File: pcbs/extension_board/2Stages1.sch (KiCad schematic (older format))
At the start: 12 parts, among them Q1 MMBT3904, Q2 MMBT3904, U1 LM324QT

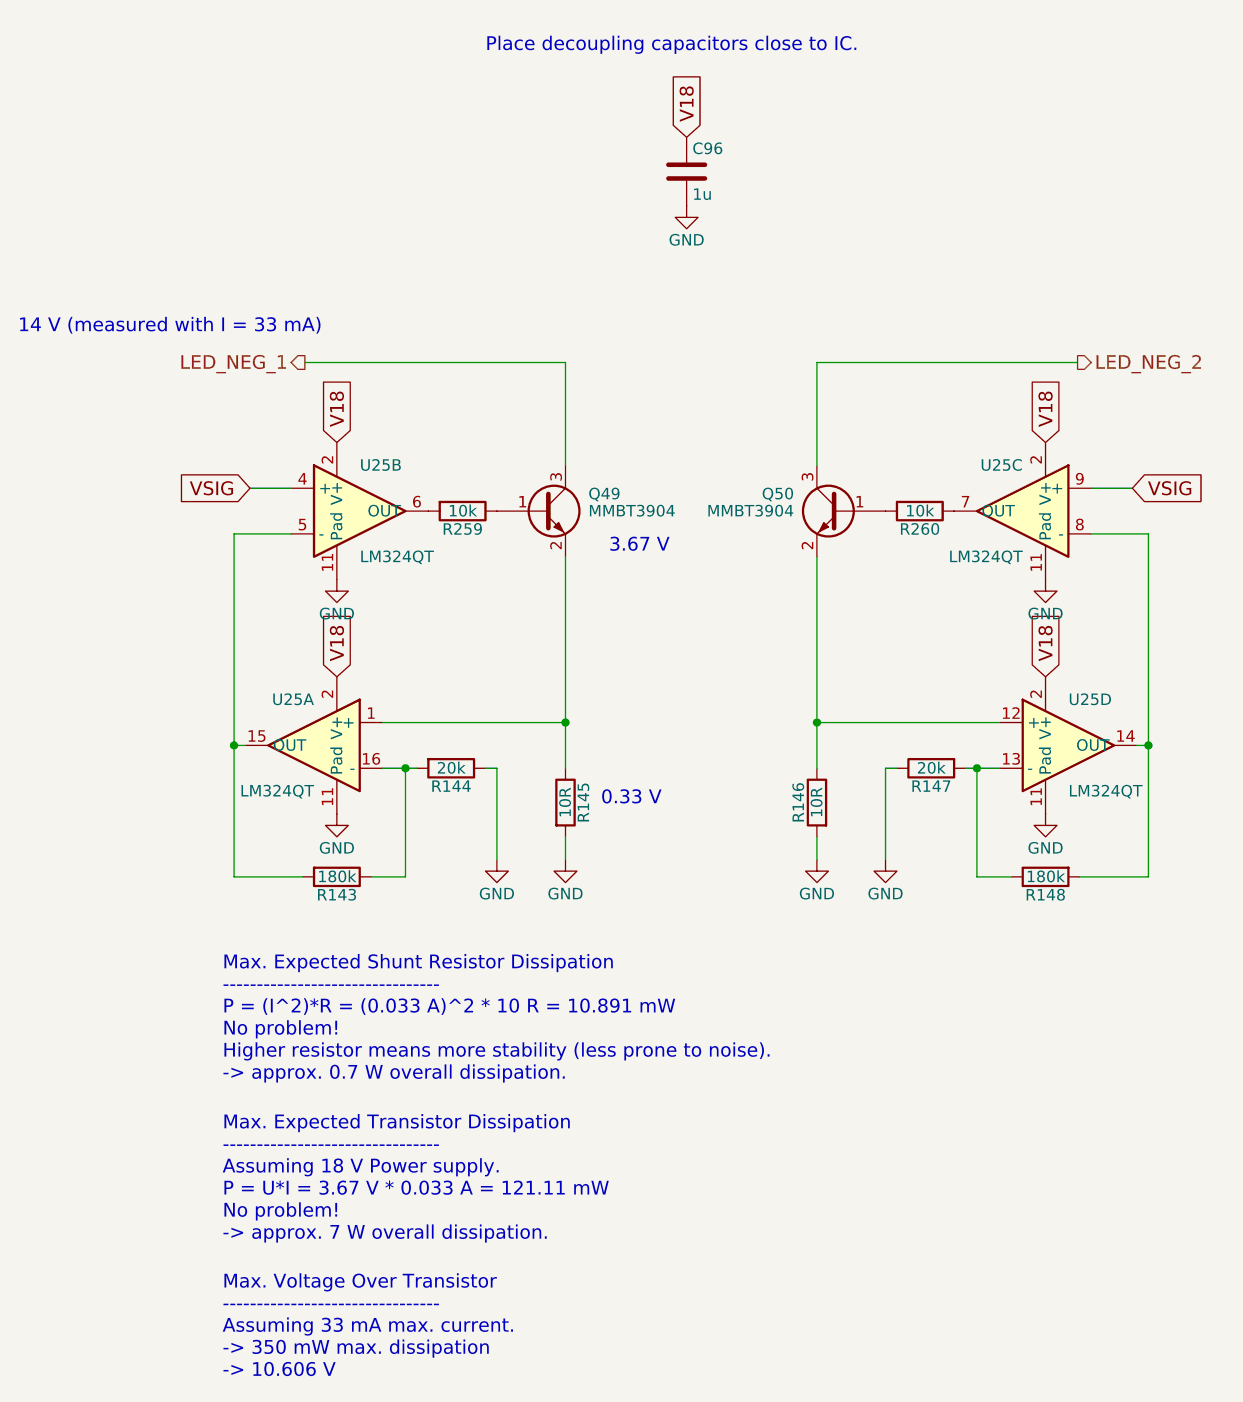
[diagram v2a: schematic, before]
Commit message: osPrintf works with signed and unsigned integers.
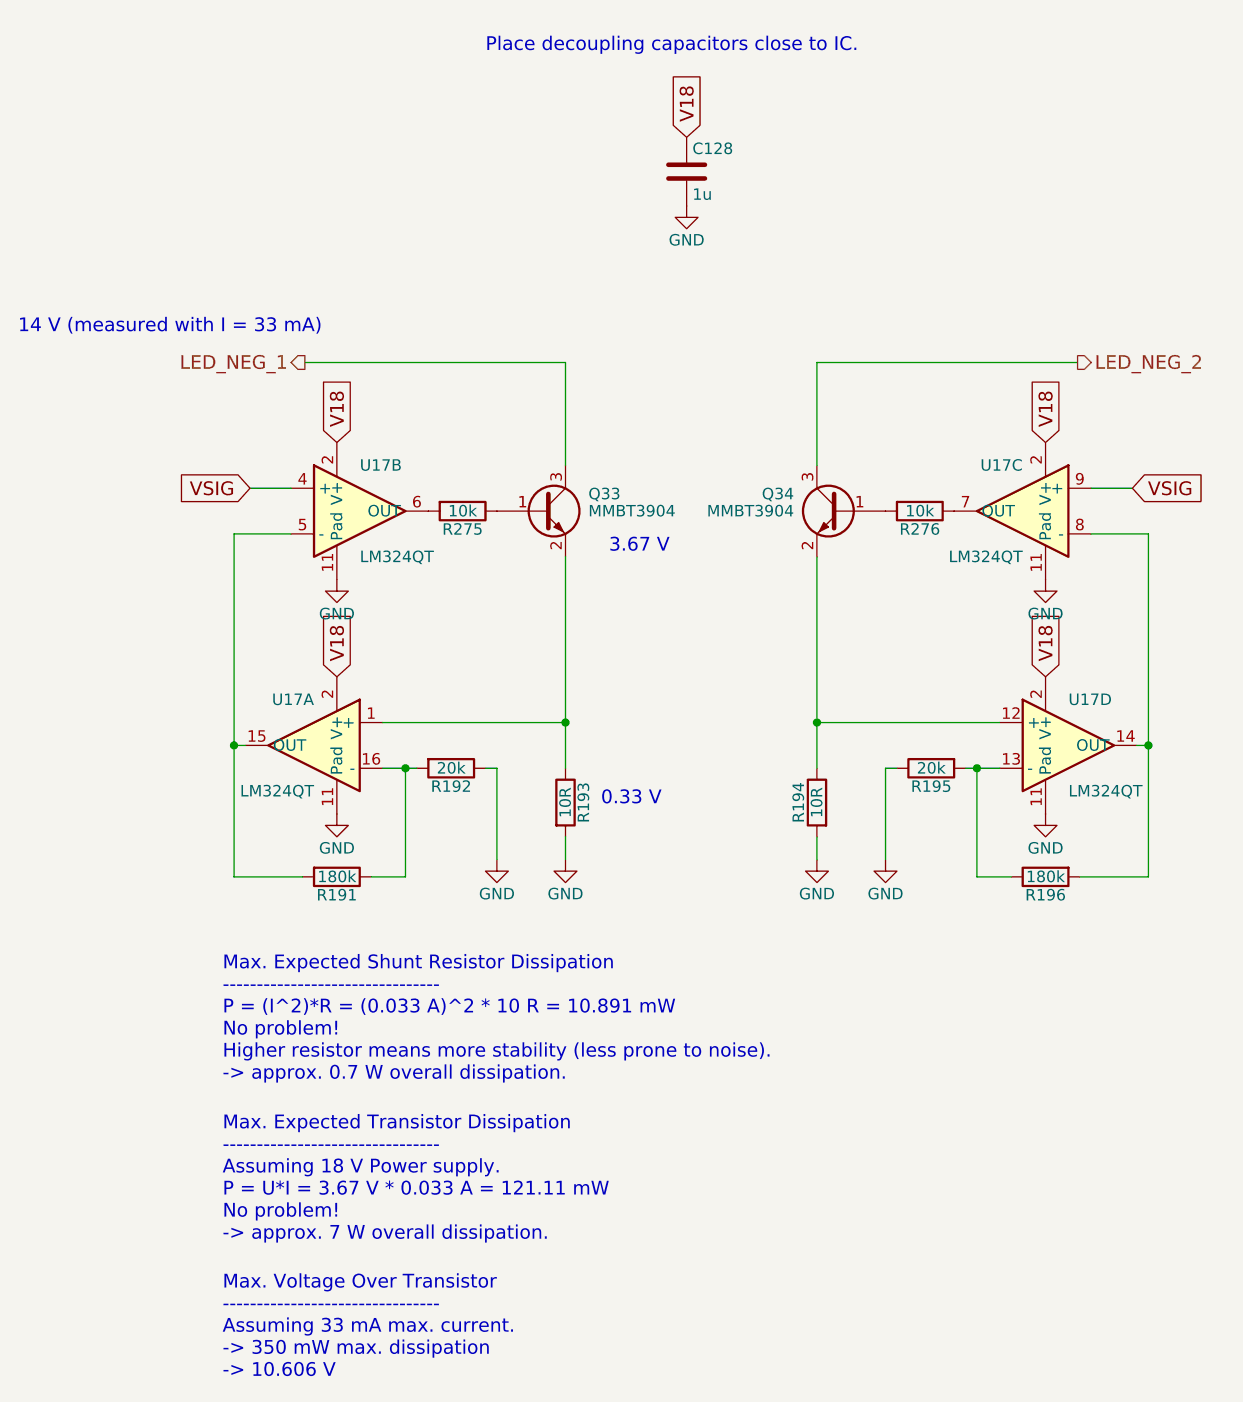
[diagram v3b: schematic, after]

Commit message: Added more OS files to be tracked. Port them now to the STM32.
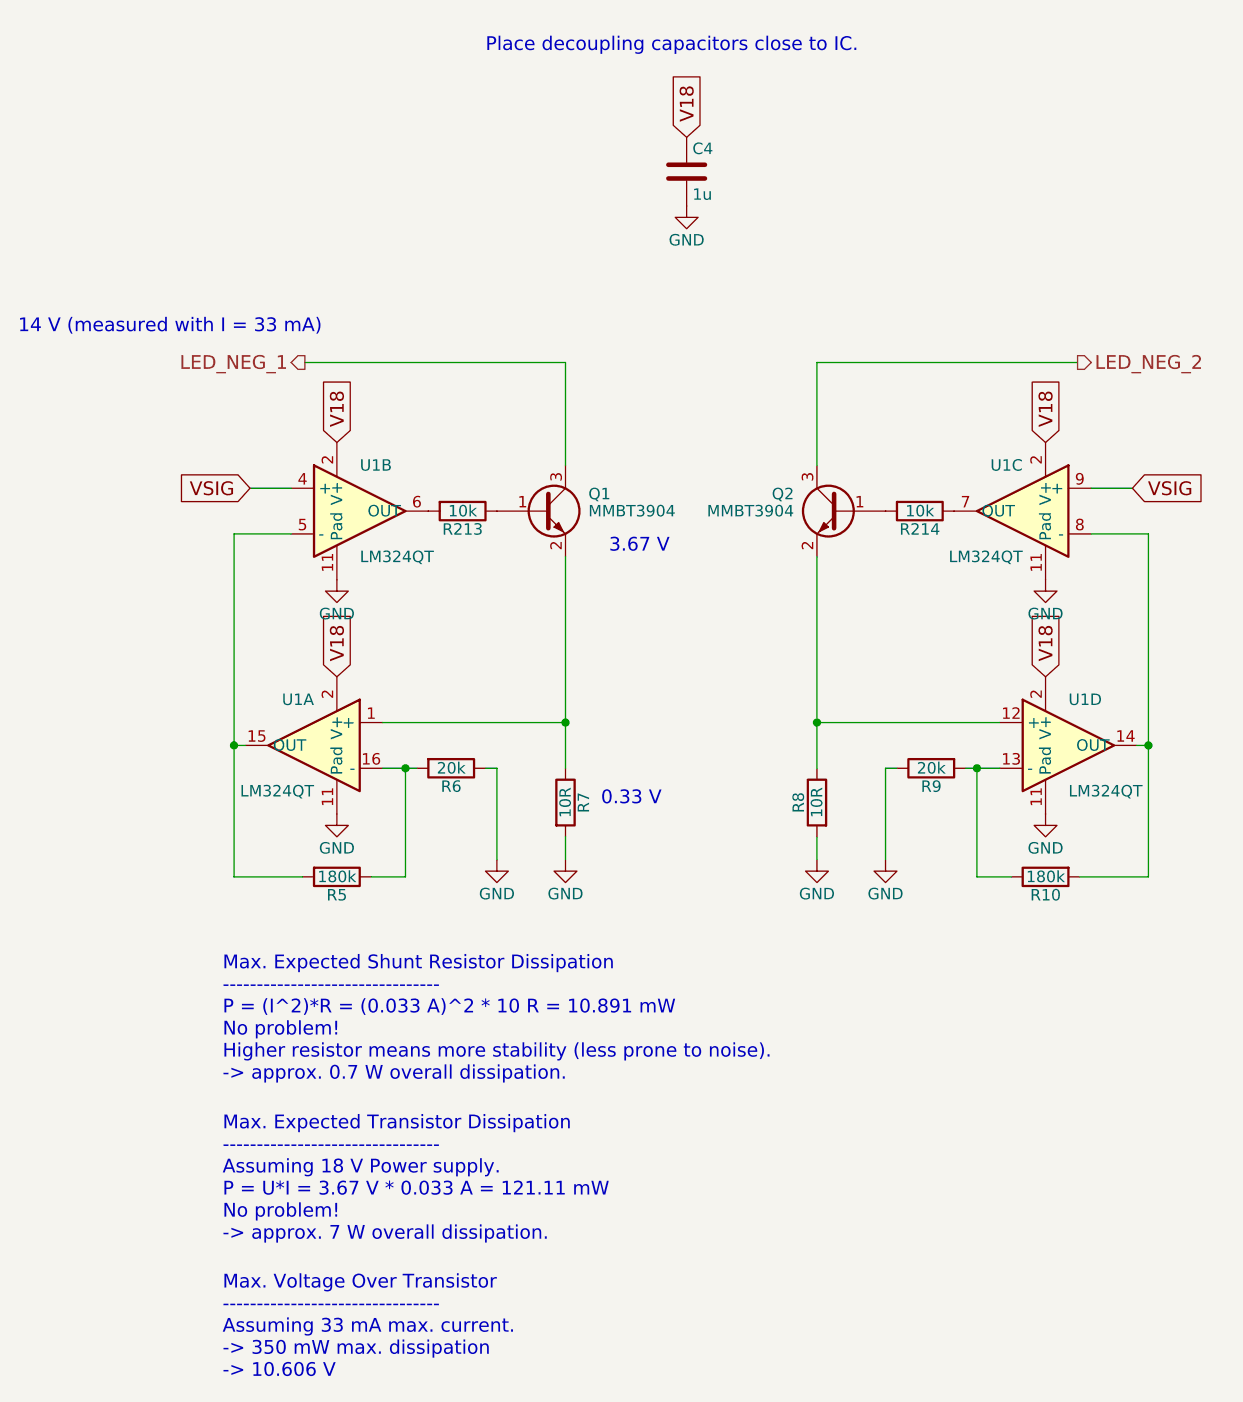
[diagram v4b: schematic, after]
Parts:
- C4: Digikey 445-5146-1-ND -> 399-3118-1-ND
